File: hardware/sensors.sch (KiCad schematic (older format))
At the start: 10 parts

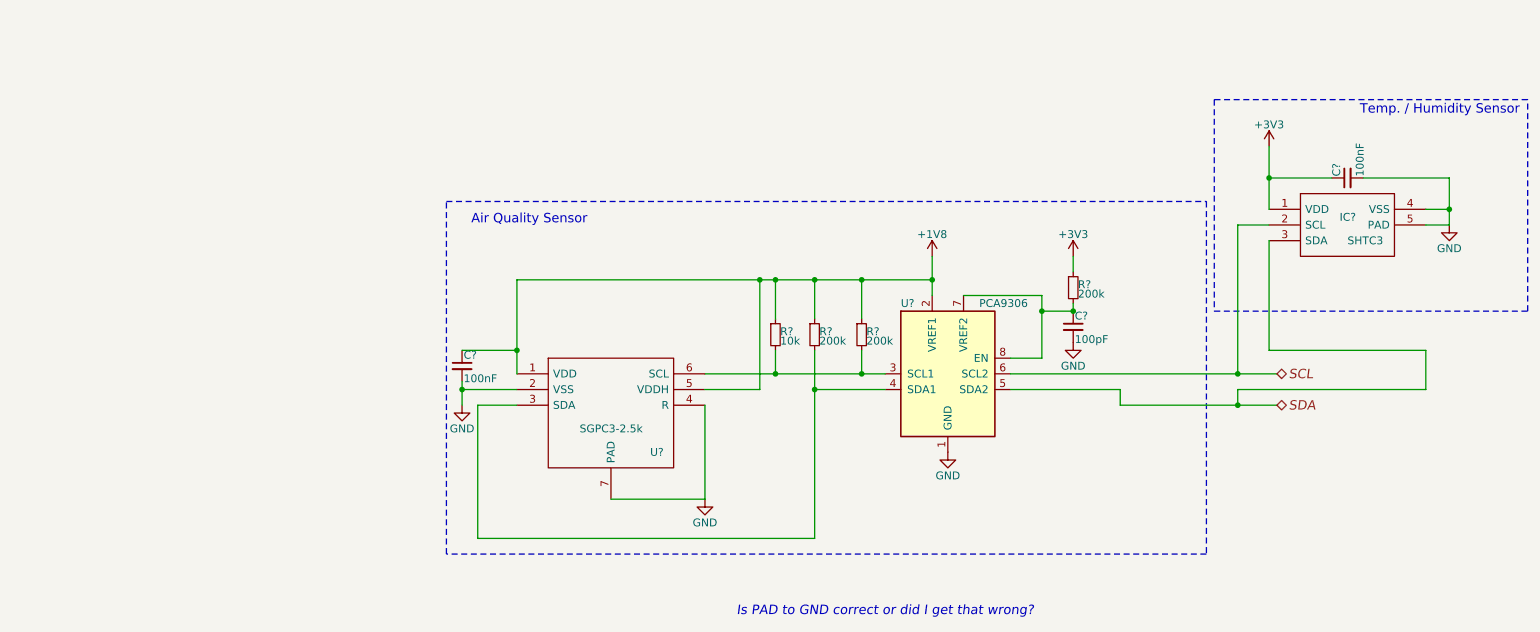
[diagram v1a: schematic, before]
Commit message: removed leftover pullup
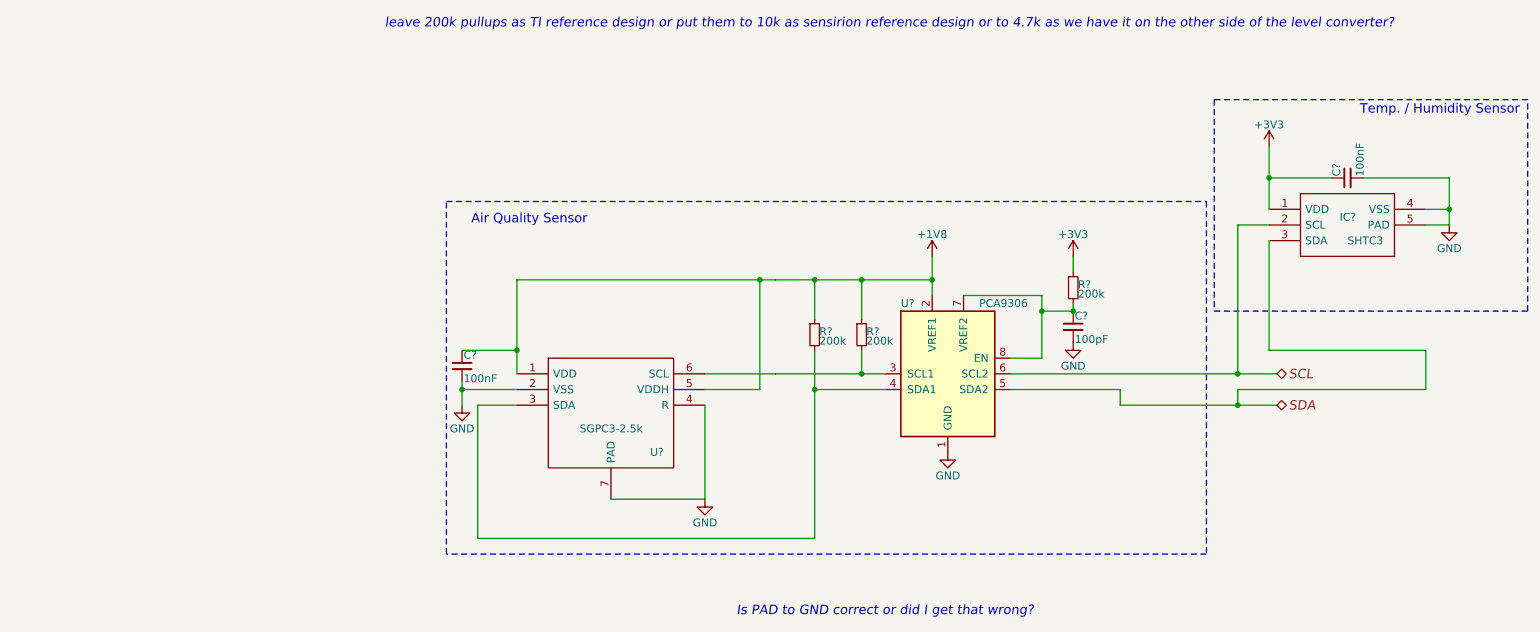
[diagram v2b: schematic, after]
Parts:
- removed R?: 10k, symbol R_Small
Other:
- note added: "leave 200k pullups as TI reference design or put them to 10k as sensirion reference design or to 4.7k as we have it on the other side of the level converter?"
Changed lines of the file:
@@
-$EndComp
-$Comp
-L R_Small R?
-U 1 1 5AD3962F
-P 4250 3950
-F 0 "R?" H 4280 3970 50  0000 L CNN
-F 1 "10k" H 4280 3910 50  0000 L CNN
-F 2 "" H 4250 3950 50  0001 C CNN
-F 3 "" H 4250 3950 50  0001 C CNN
-	1    4250 3950
-	1    0    0    -1
 $EndComp
 $Comp
@@
 $EndComp
 Wire Wire Line
-	5250 3450 5250 3700
+	5250 3450 5250 3600
+Wire Wire Line
+	5250 3600 5250 3700
 Wire Wire Line
 	5450 3700 5950 3700
 Wire Wire Line
-	5950 3700 5950 4100
+	5950 3700 5950 3800
+Wire Wire Line
+	5950 3800 5950 4100
 Wire Wire Line
 	5950 4100 5750 4100
@@
 Connection ~ 6150 3800
 Wire Wire Line
-	5750 4200 7450 4200
-Wire Wire Line
-	6450 4400 7450 4400
+	5750 4200 7200 4200
+Wire Wire Line
+	7200 4200 7450 4200
+Wire Wire Line
+	6450 4400 7200 4400
+Wire Wire Line
+	7200 4400 7450 4400
 Wire Wire Line
 	6450 4400 6450 4300
@@
 	4500 3850 4500 3600
 Wire Wire Line
-	2600 3600 5250 3600
+	2600 3600 4150 3600
+Wire Wire Line
+	4150 3600 4250 3600
+Wire Wire Line
+	4250 3600 4500 3600
+Wire Wire Line
+	4500 3600 4800 3600
+Wire Wire Line
+	4800 3600 5250 3600
 Connection ~ 5250 3600
 Wire Wire Line
@@
 Connection ~ 4800 3600
 Wire Wire Line
-	3800 4200 4950 4200
+	4800 4200 4950 4200
 Wire Wire Line
 	4800 4200 4800 4050
@@
 	4950 4300 4500 4300
 Wire Wire Line
-	4500 4050 4500 5250
+	4500 4050 4500 4300
+Wire Wire Line
+	4500 4300 4500 5250
 Connection ~ 4800 4200
 Wire Wire Line
@@
 	2350 4400 2600 4400
 Connection ~ 4500 4300
-Wire Wire Line
-	4250 4050 4250 4200
-Connection ~ 4250 4200
-Wire Wire Line
-	4250 3850 4250 3600
 Connection ~ 4500 3600
 Wire Wire Line
@@
 Wire Wire Line
 	4150 4300 4150 3600
-Connection ~ 4250 3600
 Wire Wire Line
 	3800 4400 3800 5000
@@
 	2600 4300 2250 4300
 Wire Wire Line
-	2250 4250 2250 4400
+	2250 4250 2250 4300
+Wire Wire Line
+	2250 4300 2250 4400
 Connection ~ 2250 4300
 Wire Wire Line
-	2600 3600 2600 4200
+	2600 3600 2600 4050
+Wire Wire Line
+	2600 4050 2600 4200
 Wire Wire Line
 	2600 4050 2250 4050
@@
 	7800 2950 7400 2950
 Wire Wire Line
-	7400 2750 7400 3150
+	7400 2750 7400 2950
+Wire Wire Line
+	7400 2950 7400 3150
 Connection ~ 7400 2950
 Wire Wire Line
@@
 SDA
 Wire Wire Line
-	8550 2950 8550 3250
+	8550 2950 8550 3150
+Wire Wire Line
+	8550 3150 8550 3250
 Wire Wire Line
 	3800 5000 3200 5000
@@
 	1    0    0    -1
 $EndComp
+Wire Wire Line
+	4250 4200 4800 4200
+Wire Wire Line
+	3800 4200 4250 4200
+Text Notes 8200 2000 2    60   Italic 0
+leave 200k pullups as TI reference design or put them to 10k as sensirion reference design or to 4.7k as we have it on the other side of the level converter?
 $EndSCHEMATC

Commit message: removed comment and added new question
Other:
- note removed: "Is PAD to GND correct or did I get that wrong?"
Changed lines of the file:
@@
 Sheet 2 6
 Title "IoT conference badge - mainboard"
-Date ""
+Date "2018-04-30"
 Rev "0.2.0"
 Comp "MakeZürich (makezurich.ch) & GDG Zürich (gdgzh.ch)"
@@
 Wire Wire Line
 	3800 5000 3200 5000
-Text Notes 5900 5750 2    60   Italic 0
-Is PAD to GND correct or did I get that wrong?
 Wire Wire Line
 	8550 3250 8400 3250
